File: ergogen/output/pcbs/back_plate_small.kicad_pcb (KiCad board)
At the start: 2 copper layers, 127.5 x 91.9 mm, 6 parts

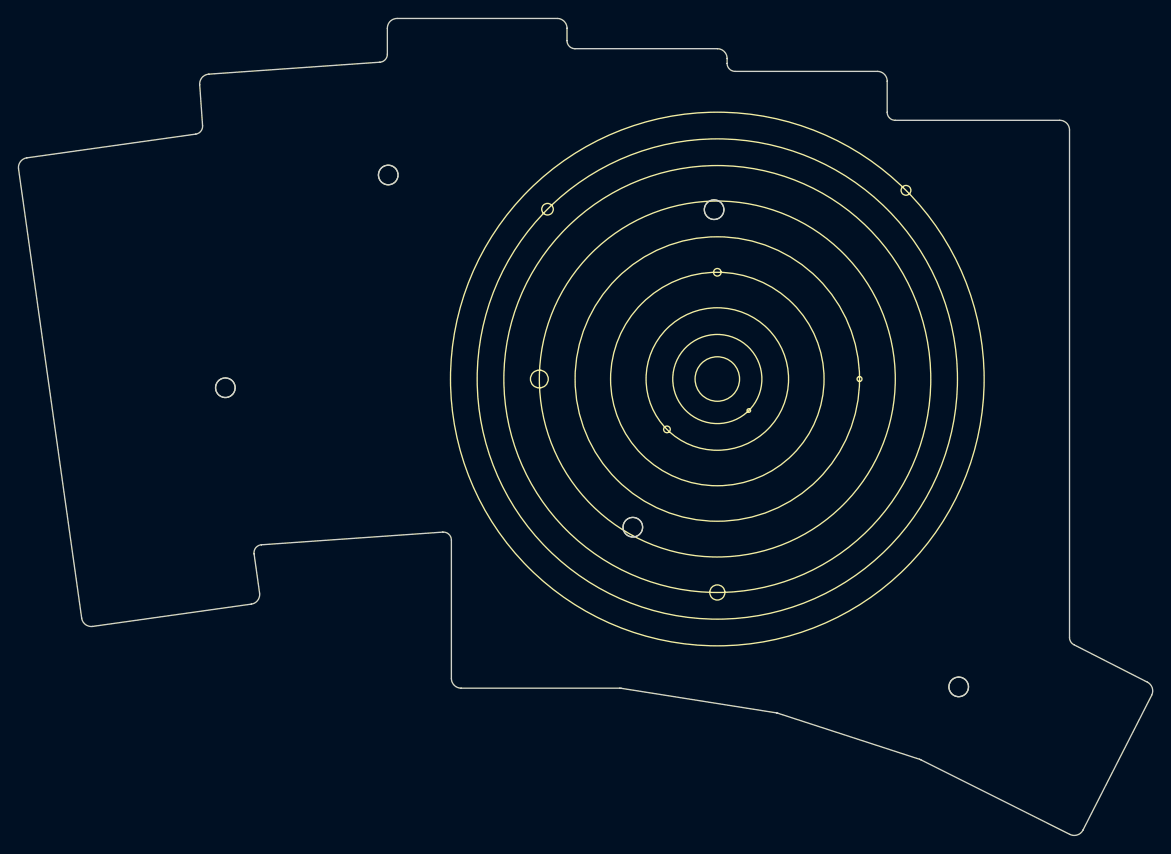
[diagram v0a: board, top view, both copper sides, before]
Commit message: case and backplate updates
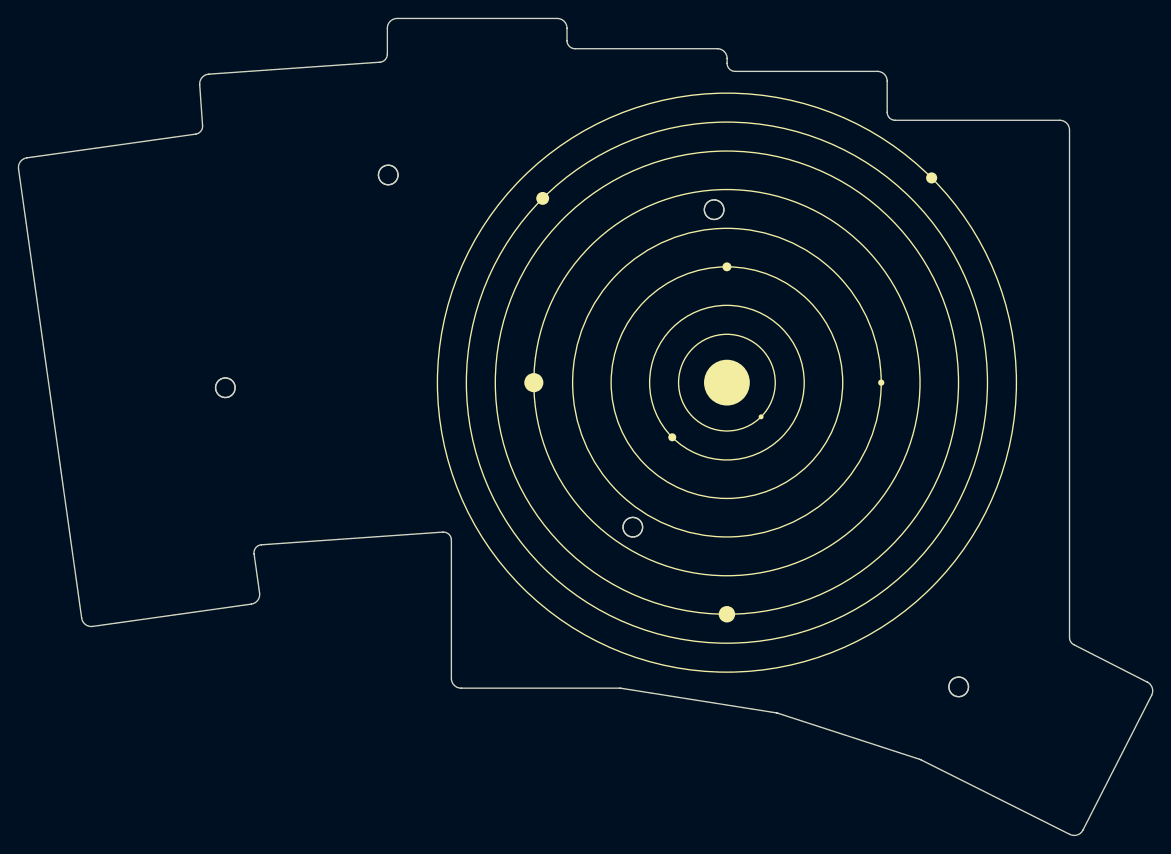
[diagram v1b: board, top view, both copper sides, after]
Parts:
- moved ? 1.15 mm to (130.4, 72.4)
